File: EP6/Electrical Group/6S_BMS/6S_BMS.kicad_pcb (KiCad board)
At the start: 4 copper layers, 100 x 70 mm, 188 parts, among them J1 battery cells, J10 I2C1, J11 CAN1, J12 frontBox, J13 USB_C_stm32, J2 GLVMS, J3 BOOT_BTN, J4 24Vout, J5 CHARGE, J6 UART2, J7 SWD, J8 7seg, J9 RESET, Q1 HSBA3119, Q10 SI2301CDS-T1-GE3, Q11 SI2301CDS-T1-GE3, Q12 SI2301CDS-T1-GE3, Q13 SI2301CDS-T1-GE3, Q14 SI2301CDS-T1-GE3, Q15 SI2301CDS-T1-GE3, Q2 2N7002, Q3 2N7002, Q4 HSBA3119, Q5 2N7002, Q6 2N7002, Q7 AO3401A, Q9 HSBA3119, SW1 RESET, U1 78L05G-AB3-R, U2 HT7533, U3 BQ7693003, U4 TCAN1042VDRQ1, U5 STM32F103C8Tx, U6 CAT24C256, U7 LM66100DCK, U8 LM74700, Y1 8MHz X49SM8MSD2SC

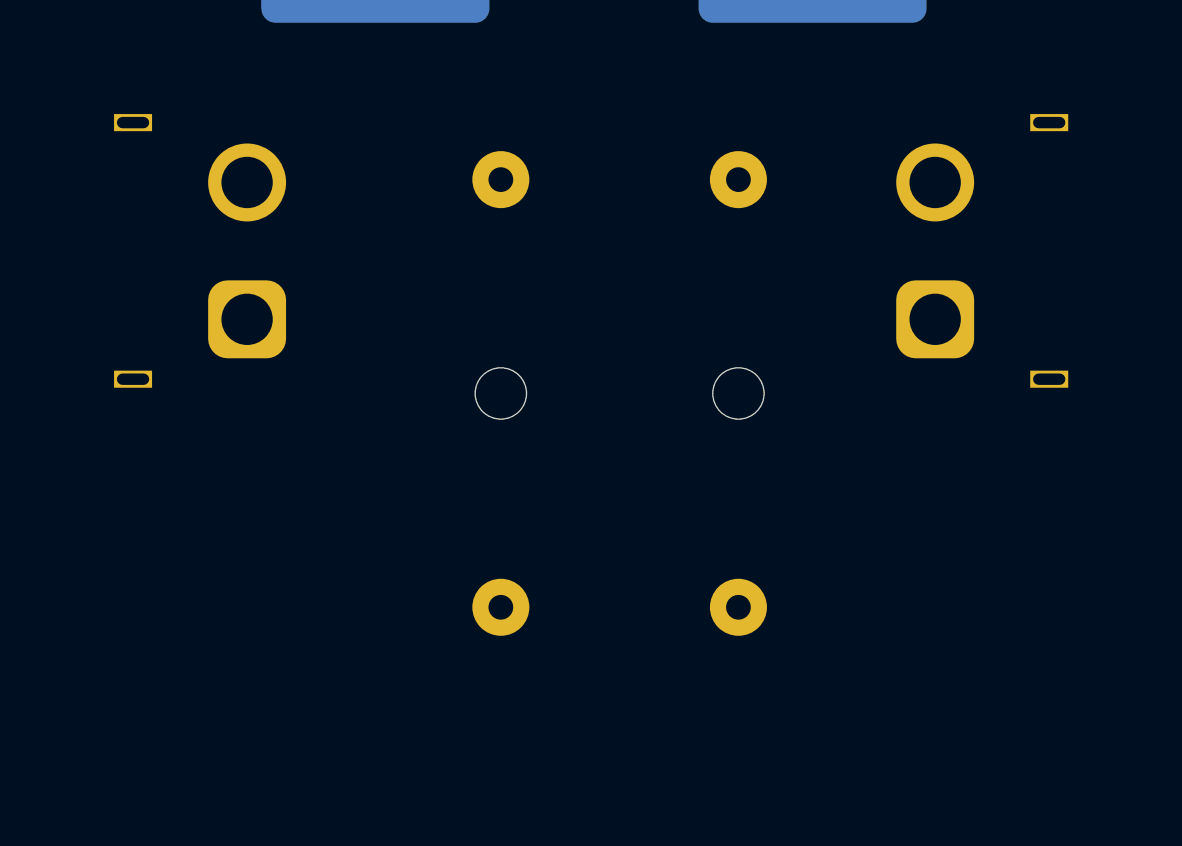
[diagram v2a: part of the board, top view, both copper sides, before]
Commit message: added 3d model for cell pack and xt60pw connectors
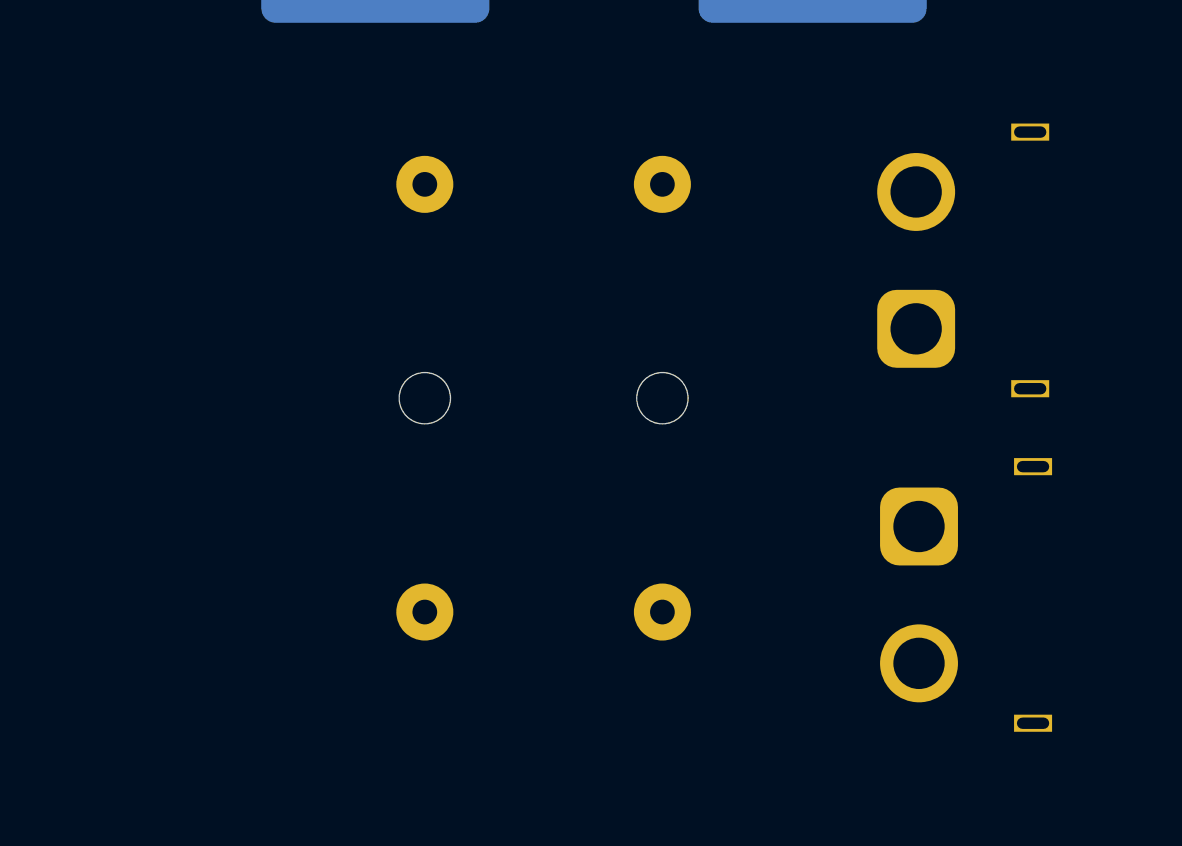
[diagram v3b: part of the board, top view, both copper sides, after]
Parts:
- moved J4 37.0 mm to (167.0, 57.0), turned to 90 degrees
- moved F1 4.01 mm to (141.0, 39.0)
- moved F2 4.01 mm to (153.5, 39.0)
- moved J5 1.12 mm to (166.8, 46.6)
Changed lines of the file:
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@@
 	(footprint "Connector_AMASS:AMASS_XT60PW-M_1x02_P7.20mm_Horizontal"
 		(layer "B.Cu")
-		(at 167.85 46.1 90)
+		(at 166.85 46.6 90)
 		(descr "Connector XT60 Horizontal PCB Female, https://www.tme.eu/en/Document/9b8d0c5eb7094295f3d3112c214d3ade/XT60PW%20SPEC.pdf")
 		(tags "RC Connector XT60")
@@
 			)
 		)
+		(model "${KIPRJMOD}/3dshapes/XT60PW_MALE.step"
+			(offset
+				(xyz 3.6 15.3 4.67)
+			)
+			(scale
+				(xyz 1 1 1)
+			)
+			(rotate
+				(xyz -90 0 0)
+			)
+		)
 	)
 	(footprint "Fuse:Fuseholder_Cylinder-5x20mm_Schurter_0031_8201_Horizontal_Open"
 		(layer "B.Cu")
-		(at 157.5 38.75 -90)
+		(at 153.5 39 -90)
 		(descr "Fuseholder horizontal open, 5x20mm, 500V, 16A, Schurter 0031.8201, https://us.schurter.com/bundles/snceschurter/epim/_ProdPool_/newDS/en/typ_OGN.pdf")
 		(tags "Fuseholder horizontal open 5x20 Schurter 0031.8201")
@@
 	(footprint "Fuse:Fuseholder_Cylinder-5x20mm_Schurter_0031_8201_Horizontal_Open"
 		(layer "B.Cu")
-		(at 145 38.75 -90)
+		(at 141 39 -90)
 		(descr "Fuseholder horizontal open, 5x20mm, 500V, 16A, Schurter 0031.8201, https://us.schurter.com/bundles/snceschurter/epim/_ProdPool_/newDS/en/typ_OGN.pdf")
 		(tags "Fuseholder horizontal open 5x20 Schurter 0031.8201")
@@
 			(layer "User.7")
 		)
-		(fp_text user "+"
-			(at 118 40 0)
+		(fp_text user "-"
+			(at 20 40 0)
 			(unlocked yes)
 			(layer "B.SilkS")
@@
 					(thickness 0.5)
 				)
-				(justify right bottom mirror)
+				(justify left bottom mirror)
 			)
 		)
-		(fp_text user "-"
-			(at 20 40 0)
+		(fp_text user "+"
+			(at 118 40 0)
 			(unlocked yes)
 			(layer "B.SilkS")
@@
 					(thickness 0.5)
 				)
-				(justify left bottom mirror)
+				(justify right bottom mirror)
 			)
 		)
@@
 			(thermal_bridge_angle 45)
 		)
+		(model "${KIPRJMOD}/cell_pack.step"
+			(offset
+				(xyz 138 35 -52)
+			)
+			(scale
+				(xyz 1 1 1)
+			)
+			(rotate
+				(xyz -90 0 180)
+			)
+		)
 	)
 	(footprint "Connector_JST:JST_PH_S5B-PH-K_1x05_P2.00mm_Horizontal"
@@
 	(footprint "Connector_AMASS:AMASS_XT60PW-F_1x02_P7.20mm_Horizontal"
 		(layer "B.Cu")
-		(at 131.65 46.1 -90)
+		(at 167 57 90)
 		(descr "Connector XT60 Horizontal PCB Female, https://www.tme.eu/en/Document/9b8d0c5eb7094295f3d3112c214d3ade/XT60PW%20SPEC.pdf")
 		(tags "RC Connector XT60")
@@
 		)
 		(property "Footprint" "Connector_AMASS:AMASS_XT60PW-F_1x02_P7.20mm_Horizontal"
-			(at 0 0 90)
+			(at 0 0 -90)
 			(unlocked yes)
 			(layer "B.Fab")
@@
 		)
 		(property "Datasheet" ""
-			(at 0 0 90)
+			(at 0 0 -90)
 			(unlocked yes)
 			(layer "B.Fab")
@@
 		)
 		(property "Description" "Generic connector, single row, 01x02, script generated (kicad-library-utils/schlib/autogen/connector/)"
-			(at 0 0 90)
+			(at 0 0 -90)
 			(unlocked yes)
 			(layer "B.Fab")
@@
 		(attr through_hole)
 		(fp_line
-			(start 3.41 15.46)
-			(end -10.61 15.46)
+			(start -2.31 -1.96)
+			(end -6.05 -1.96)
 			(stroke
 				(width 0.12)
@@
 		)
 		(fp_line
-			(start -10.61 7.76)
-			(end -10.61 15.46)
+			(start 4.26 2.15)
+			(end 4.26 7.76)
 			(stroke
 				(width 0.12)
@@
 		)
 		(fp_line
-			(start -10.61 7.76)
+			(start -11.46 2.15)
 			(end -11.46 7.76)
 			(stroke
@@
 		)
 		(fp_line
-			(start 3.41 7.76)
-			(end 3.41 15.46)
+			(start 4.26 7.76)
+			(end 3.41 7.76)
 			(stroke
 				(width 0.12)
@@
 		)
 		(fp_line
-			(start 4.26 7.76)
-			(end 3.41 7.76)
+			(start 3.41 7.76)
+			(end 3.41 15.46)
 			(stroke
 				(width 0.12)
@@
 		)
 		(fp_line
-			(start -11.46 2.15)
+			(start -10.61 7.76)
 			(end -11.46 7.76)
 			(stroke
@@
 		)
 		(fp_line
-			(start 4.26 2.15)
-			(end 4.26 7.76)
+			(start -10.61 7.76)
+			(end -10.61 15.46)
 			(stroke
 				(width 0.12)
@@
 		)
 		(fp_line
-			(start -2.31 -1.96)
-			(end -6.05 -1.96)
+			(start 3.41 15.46)
+			(end -10.61 15.46)
 			(stroke
 				(width 0.12)
@@
 		)
 		(fp_arc
-			(start -11.46 2.15)
-			(mid -10.677645 -0.302568)
-			(end -8.5899 -1.808718)
+			(start 2.266806 -1.372958)
+			(mid 3.727162 0.126139)
+			(end 4.26 2.15)
 			(stroke
 				(width 0.12)
@@
 		)
 		(fp_arc
-			(start 2.266806 -1.372958)
-			(mid 3.727162 0.126139)
-			(end 4.26 2.15)
+			(start -11.46 2.15)
+			(mid -10.677645 -0.302568)
+			(end -8.5899 -1.808718)
 			(stroke
 				(width 0.12)
@@
 		)
 		(fp_line
-			(start 4.65 15.85)
-			(end -11.85 15.85)
+			(start -11.85 -2.55)
+			(end 4.65 -2.55)
 			(stroke
 				(width 0.05)
@@
 		)
 		(fp_line
-			(start 4.65 15.85)
-			(end 4.65 -2.55)
+			(start -11.85 -2.55)
+			(end -11.85 15.85)
 			(stroke
 				(width 0.05)
@@
 		)
 		(fp_line
-			(start -11.85 -2.55)
-			(end -11.85 15.85)
+			(start 4.65 15.85)
+			(end 4.65 -2.55)
 			(stroke
 				(width 0.05)
@@
 		)
 		(fp_line
-			(start -11.85 -2.55)
-			(end 4.65 -2.55)
+			(start 4.65 15.85)
+			(end -11.85 15.85)
 			(stroke
 				(width 0.05)
@@
 		)
 		(fp_line
-			(start -10.5 15.35)
-			(end -10.5 7.65)
+			(start 0.15 -1.85)
+			(end -7.35 -1.85)
 			(stroke
 				(width 0.1)
@@
 		)
 		(fp_line
-			(start 3.3 15.35)
-			(end -10.5 15.35)
+			(start 4.15 2.15)
+			(end 4.15 7.65)
 			(stroke
 				(width 0.1)
@@
 		)
 		(fp_line
-			(start 3.3 15.35)
-			(end 3.3 7.65)
+			(start -11.35 2.15)
+			(end -11.35 7.65)
 			(stroke
 				(width 0.1)
@@
 		)
 		(fp_line
-			(start -11.35 2.15)
-			(end -11.35 7.65)
+			(start 3.3 15.35)
+			(end 3.3 7.65)
 			(stroke
 				(width 0.1)
@@
 		)
 		(fp_line
-			(start 4.15 2.15)
-			(end 4.15 7.65)
+			(start 3.3 15.35)
+			(end -10.5 15.35)
 			(stroke
 				(width 0.1)
@@
 		)
 		(fp_line
-			(start 0.15 -1.85)
-			(end -7.35 -1.85)
+			(start -10.5 15.35)
+			(end -10.5 7.65)
 			(stroke
 				(width 0.1)
@@
 		)
 		(fp_arc
-			(start -11.35 2.15)
-			(mid -10.203176 -0.688678)
-			(end -7.385 -1.885)
+			(start 0.15 -1.85)
+			(mid 2.978427 -0.678427)
+			(end 4.15 2.15)
 			(stroke
 				(width 0.1)
@@
 		)
 		(fp_arc
-			(start 0.15 -1.85)
-			(mid 2.978427 -0.678427)
-			(end 4.15 2.15)
+			(start -11.35 2.15)
+			(mid -10.203176 -0.688678)
+			(end -7.385 -1.885)
 			(stroke
 				(width 0.1)
@@
 		)
 		(pad "" thru_hole rect
-			(at -10.35 6 270)
+			(at -10.35 6 90)
 			(size 0.9 2)
 			(drill oval 0.6 1.7)
@@
 		)
 		(pad "" thru_hole rect
-			(at 3.15 6 270)
+			(at 3.15 6 90)
 			(size 0.9 2)
 			(drill oval 0.6 1.7)
@@
 		)
 		(pad "1" thru_hole roundrect
-			(at 0 0 270)
+			(at 0 0 90)
 			(size 4.1 4.1)
 			(drill 2.7)
@@
 		)
 		(pad "2" thru_hole circle
-			(at -7.2 0 270)
+			(at -7.2 0 90)
 			(size 4.1 4.1)
 			(drill 2.7)
@@
 			)
 		)
+		(model "${KIPRJMOD}/3dshapes/XT60PW_FEMALE.step"
+			(offset
+				(xyz -3.6 15.3 4.51)
+			)
+			(scale
+				(xyz 1 1 1)
+			)
+			(rotate
+				(xyz -90 180 0)
+			)
+		)
